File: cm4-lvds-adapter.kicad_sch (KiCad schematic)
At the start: 58 parts, among them J1 Plug_Molex_SlimStack_2x15_538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, J2 JST_SM_1x10_SM10B-SURS-TF-LF-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, J3 Conn_FFC_Amphenol_62684-40210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, U2 NTS0104_DHVQFN, U3 SN65DSI84

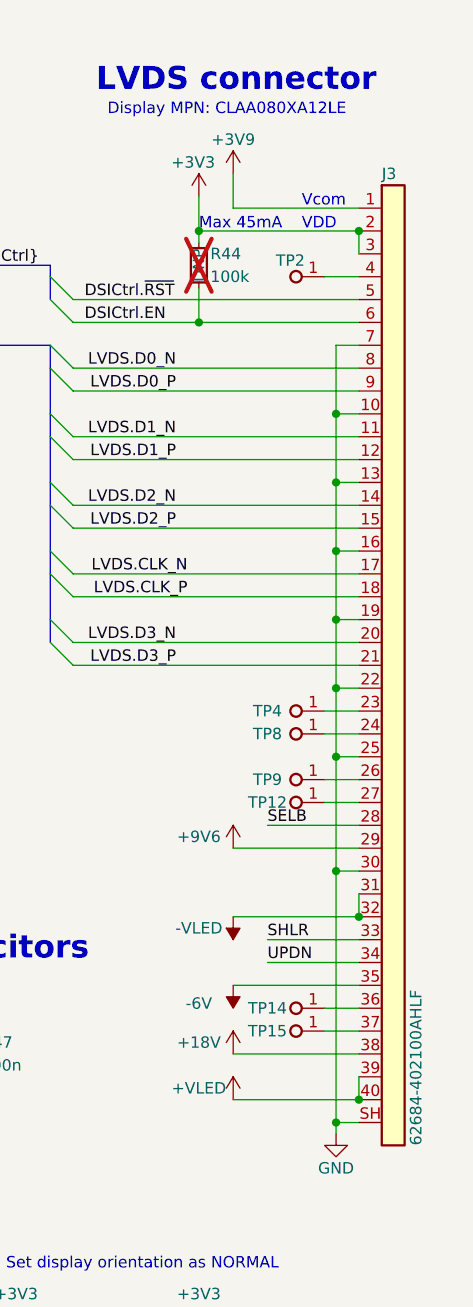
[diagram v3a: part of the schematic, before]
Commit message: [#55111] Change FFC on schematic
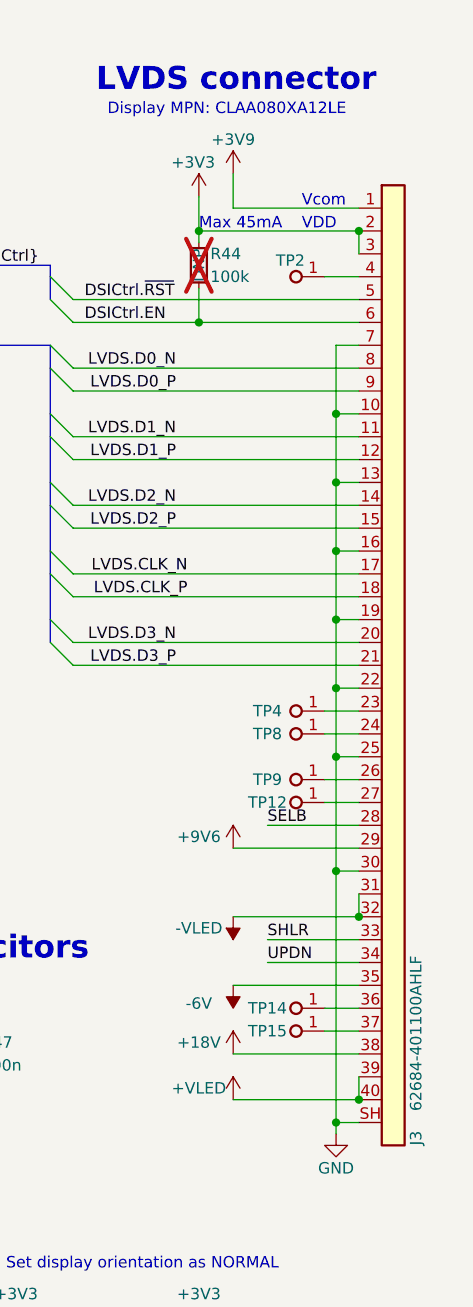
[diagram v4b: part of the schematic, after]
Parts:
- removed J3: Conn_FFC_Amphenol_62684-402100AHLF, antmicro-footprints:Conn_FFC_Amphenol_1x40_62684-402100AHLF, symbol antmicroFCCConnectors:FFC_Amphenol_1x40_62684-402100AHLF
- added J3: FFC_Amphenol_1x40_62684-401100AHLF, antmicro-footprints:Conn_FFC_Amphenol_1x40_62684-401100AHLF, symbol antmicroFCCConnectors:FFC_Amphenol_1x40_62684-401100AHLF
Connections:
- net +18V: now also J3.38
- net +3V3: now also J3.2, J3.3
- net +3V9: now also J3.1
- net +9V6: now also J3.29
- net +VLED: now also J3.39, J3.40
- net -6V: now also J3.35
- net -VLED: now also J3.31, J3.32
- net DSICtrl.EN: now also J3.6
- net DSICtrl.~{RST}: now also J3.5
- net GND: now also J3.10, J3.13, J3.16, J3.19, J3.22, J3.25, J3.30, J3.7, J3.SH
- net LVDS.CLK_N: now also J3.17
- net LVDS.CLK_P: now also J3.18
- net LVDS.D0_N: now also J3.8
- net LVDS.D0_P: now also J3.9
- net LVDS.D1_N: now also J3.11
- net LVDS.D1_P: now also J3.12
- net LVDS.D2_N: now also J3.14
- net LVDS.D2_P: now also J3.15
- net LVDS.D3_N: now also J3.20
- net LVDS.D3_P: now also J3.21
- net SELB: now also J3.28
- net SHLR: now also J3.33
- net UPDN: now also J3.34
- net at TP9.1: now also J3.26
- net at TP8.1: now also J3.24
- net at TP15.1: now also J3.37
- net at TP4.1: now also J3.23
- net at TP12.1: now also J3.27
- net at TP14.1: now also J3.36
- net at TP2.1: now also J3.4
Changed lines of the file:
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@@
   (junction (at 58.42 190.5) (diameter 0) (color 0 0 0 0)
   )
+  (junction (at 392.43 196.85) (diameter 0) (color 0 0 0 0)
+  )
   (junction (at 389.89 143.51) (diameter 0) (color 0 0 0 0)
   )
@@
   (junction (at 389.89 128.27) (diameter 0) (color 0 0 0 0)
   )
-  (junction (at 392.43 176.53) (diameter 0) (color 0 0 0 0)
-  )
   (junction (at 374.65 110.49) (diameter 0) (color 0 0 0 0)
   )
@@
   (junction (at 156.21 187.96) (diameter 0) (color 0 0 0 0)
   )
+  (junction (at 392.43 176.53) (diameter 0) (color 0 0 0 0)
+  )
   (junction (at 332.74 232.41) (diameter 0) (color 0 0 0 0)
   )
@@
   (junction (at 45.72 99.06) (diameter 0) (color 0 0 0 0)
   )
-  (junction (at 392.43 196.85) (diameter 0) (color 0 0 0 0)
-  )
   (junction (at 45.72 76.2) (diameter 0) (color 0 0 0 0)
   )
@@
     )
   )
-  (symbol (lib_id "antmicroFCCConnectors:FFC_Amphenol_1x40_62684-402100AHLF") (at 392.43 97.79 0) (unit 1)
-    (in_bom yes) (on_board yes) (dnp no)
-    (property "Reference" "J3" (at 394.97 93.98 0)
-      (effects (font (size 1.27 1.27) (thickness 0.15)) (justify left))
-    )
-    (property "Value" "Conn_FFC_Amphenol_62684-402100AHLF" (at 419.1 105.41 0)
-      (effects (font (size 1.27 1.27) (thickness 0.15)) (justify left bottom) hide)
-    )
-    (property "Footprint" "antmicro-footprints:Conn_FFC_Amphenol_1x40_62684-402100AHLF" (at 414.02 107.95 0)
-      (effects (font (size 1.27 1.27) (thickness 0.15)) (justify left bottom) hide)
-    )
-    (property "Datasheet" "https://cdn.amphenol-cs.com/media/wysiwyg/files/drawing/62684.pdf" (at 414.02 110.49 0)
-      (effects (font (size 1.27 1.27) (thickness 0.15)) (justify left bottom) hide)
-    )
-    (property "MPN" "62684-402100AHLF" (at 398.78 201.93 90)
-      (effects (font (size 1.27 1.27) (thickness 0.15)) (justify left))
-    )
-    (property "Manufacturer" "Amphenol" (at 414.02 113.03 0)
-      (effects (font (size 1.27 1.27) (thickness 0.15)) (justify left bottom) hide)
-    )
-    (property "Author" "Antmicro" (at 414.02 115.57 0)
-      (effects (font (size 1.27 1.27) (thickness 0.15)) (justify left bottom) hide)
-    )
-    (property "License" "Apache-2.0" (at 414.02 118.11 0)
-      (effects (font (size 1.27 1.27) (thickness 0.15)) (justify left bottom) hide)
-    )
-    (pin "1")
-    (pin "10")
-    (pin "11")
-    (pin "12")
-    (pin "13")
-    (pin "14")
-    (pin "15")
-    (pin "16")
-    (pin "17")
-    (pin "18")
-    (pin "19")
-    (pin "2")
-    (pin "20")
-    (pin "21")
-    (pin "22")
-    (pin "23")
-    (pin "24")
-    (pin "25")
-    (pin "26")
-    (pin "27")
-    (pin "28")
-    (pin "29")
-    (pin "3")
-    (pin "30")
-    (pin "31")
-    (pin "32")
-    (pin "33")
-    (pin "34")
-    (pin "35")
-    (pin "36")
-    (pin "37")
-    (pin "38")
-    (pin "39")
-    (pin "4")
-    (pin "40")
-    (pin "5")
-    (pin "6")
-    (pin "7")
-    (pin "8")
-    (pin "9")
-    (pin "SH")
-    (instances
-      (project "cm4-lvds-adapter"
-        (path "/60b842dc-0853-4a25-99ac-5784ddf94d0d"
-          (reference "J3") (unit 1)
-        )
-      )
-    )
-  )
   (symbol (lib_id "antmicropower:+VLED") (at 337.82 187.96 0) (unit 1)
     (in_bom yes) (on_board yes) (dnp no)
@@
         )
       )
+    )
+  )
+  (symbol (lib_id "antmicroFCCConnectors:FFC_Amphenol_1x40_62684-401100AHLF") (at 392.43 97.79 0) (unit 1)
+    (in_bom yes) (on_board yes) (dnp no)
+    (property "Reference" "J3" (at 398.78 201.93 90)
+      (effects (font (size 1.27 1.27) (thickness 0.15)) (justify left))
+    )
+    (property "Value" "FFC_Amphenol_1x40_62684-401100AHLF" (at 414.02 105.41 0)
+      (effects (font (size 1.27 1.27) (thickness 0.15)) (justify left bottom) hide)
+    )
+    (property "Footprint" "antmicro-footprints:Conn_FFC_Amphenol_1x40_62684-401100AHLF" (at 414.02 107.95 0)
+      (effects (font (size 1.27 1.27) (thickness 0.15)) (justify left bottom) hide)
+    )
+    (property "Datasheet" "https://cdn.amphenol-cs.com/media/wysiwyg/files/drawing/62684.pdf" (at 414.02 110.49 0)
+      (effects (font (size 1.27 1.27) (thickness 0.15)) (justify left bottom) hide)
+    )
+    (property "MPN" "62684-401100AHLF" (at 398.78 198.12 90)
+      (effects (font (size 1.27 1.27) (thickness 0.15)) (justify left))
+    )
+    (property "Manufacturer" "Amphenol" (at 414.02 113.03 0)
+      (effects (font (size 1.27 1.27) (thickness 0.15)) (justify left bottom) hide)
+    )
+    (property "Author" "Antmicro" (at 414.02 115.57 0)
+      (effects (font (size 1.27 1.27) (thickness 0.15)) (justify left bottom) hide)
+    )
+    (property "License" "Apache-2.0" (at 414.02 118.11 0)
+      (effects (font (size 1.27 1.27) (thickness 0.15)) (justify left bottom) hide)
+    )
+    (pin "26")
+    (pin "35")
+    (pin "37")
+    (pin "1")
+    (pin "39")
+    (pin "36")
+    (pin "6")
+    (pin "31")
+    (pin "21")
+    (pin "40")
+    (pin "12")
+    (pin "17")
+    (pin "34")
+    (pin "23")
+    (pin "8")
+    (pin "25")
+    (pin "19")
+    (pin "28")
+    (pin "16")
+    (pin "4")
+    (pin "2")
+    (pin "33")
+    (pin "38")
+    (pin "7")
+    (pin "9")
+    (pin "3")
+    (pin "20")
+    (pin "15")
+    (pin "18")
+    (pin "11")
+    (pin "29")
+    (pin "27")
+    (pin "13")
+    (pin "14")
+    (pin "32")
+    (pin "5")
+    (pin "24")
+    (pin "10")
+    (pin "30")
+    (pin "SH")
+    (pin "22")
+    (instances
+      (project "cm4-lvds-adapter"
+        (path "/60b842dc-0853-4a25-99ac-5784ddf94d0d"
+          (reference "J3") (unit 1)
+        )
+      )

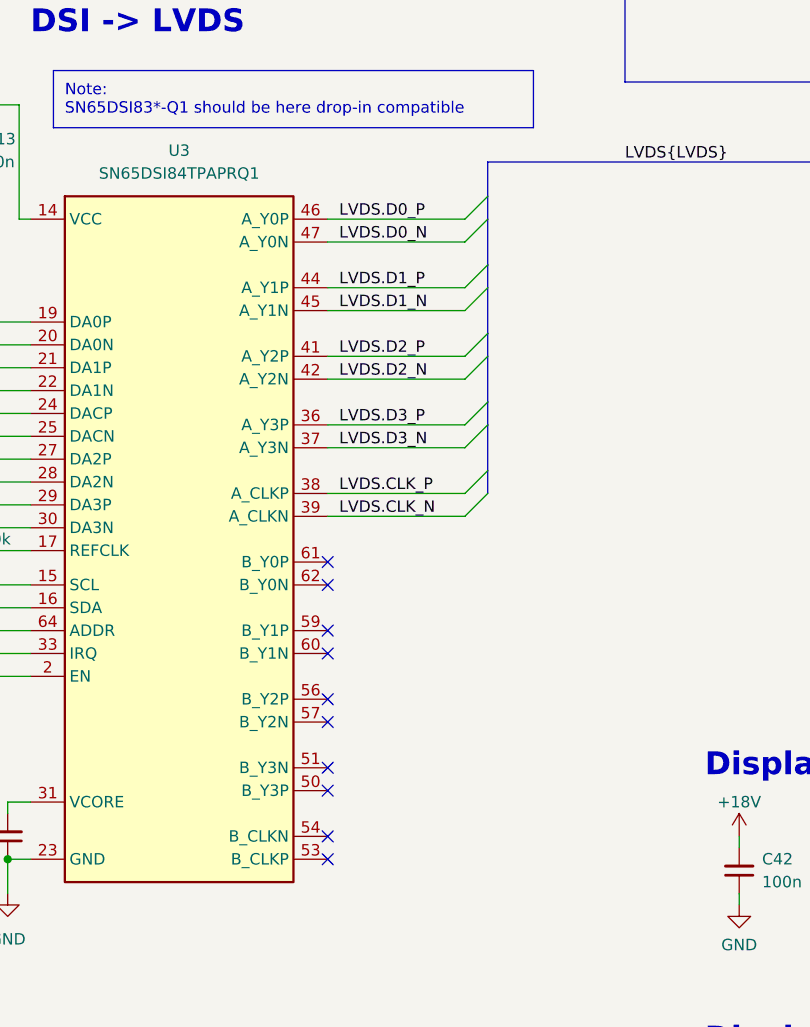
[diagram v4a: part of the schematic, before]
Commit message: [#55272] Change layout of the SN65DSI84-Q1
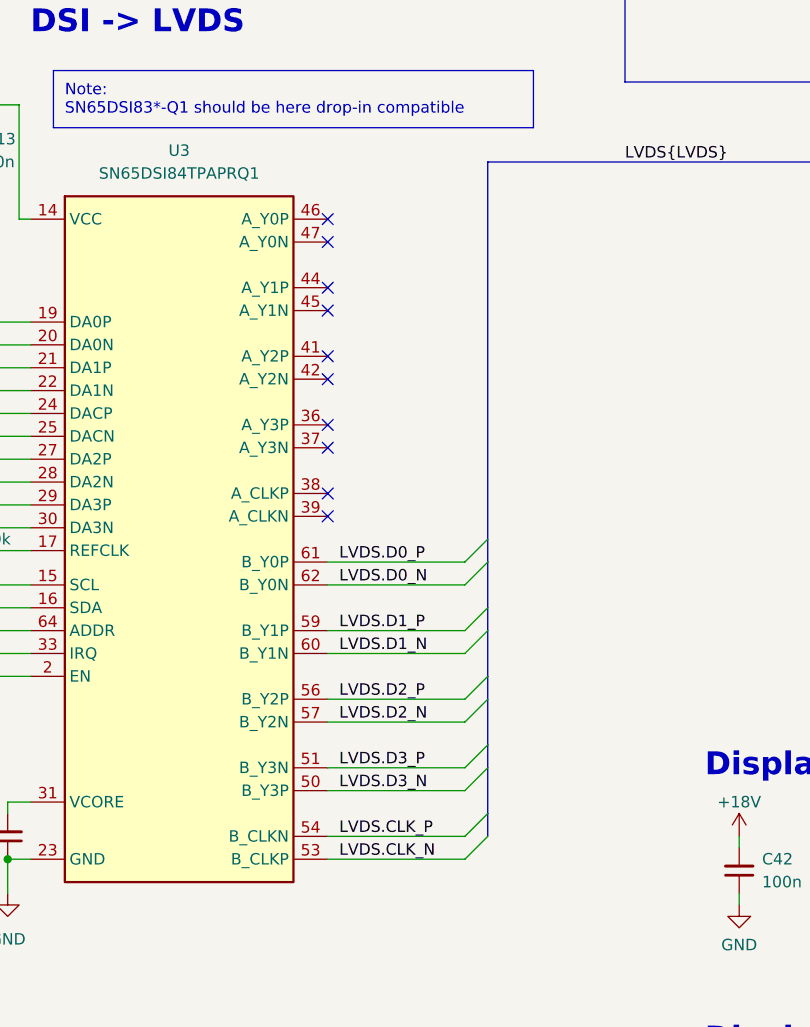
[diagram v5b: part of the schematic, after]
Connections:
- net LVDS.CLK_N: now also U3.53 (B_CLKP); no longer U3.39 (A_CLKN)
- net LVDS.CLK_P: now also U3.54 (B_CLKN); no longer U3.38 (A_CLKP)
- net LVDS.D0_N: now also U3.62 (B_Y0N); no longer U3.47 (A_Y0N)
- net LVDS.D0_P: now also U3.61 (B_Y0P); no longer U3.46 (A_Y0P)
- net LVDS.D1_N: now also U3.60 (B_Y1N); no longer U3.45 (A_Y1N)
- net LVDS.D1_P: now also U3.59 (B_Y1P); no longer U3.44 (A_Y1P)
- net LVDS.D2_N: now also U3.57 (B_Y2N); no longer U3.42 (A_Y2N)
- net LVDS.D2_P: now also U3.56 (B_Y2P); no longer U3.41 (A_Y2P)
- net LVDS.D3_N: now also U3.50 (B_Y3P); no longer U3.37 (A_Y3N)
- net LVDS.D3_P: now also U3.51 (B_Y3N); no longer U3.36 (A_Y3P)
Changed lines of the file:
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@@
   (no_connect (at 58.42 111.76))
   (no_connect (at 58.42 109.22))
-  (no_connect (at 261.62 157.48))
-  (no_connect (at 261.62 165.1))
-  (no_connect (at 261.62 180.34))
-  (no_connect (at 261.62 172.72))
-  (no_connect (at 261.62 175.26))
+  (no_connect (at 261.62 119.38))
+  (no_connect (at 261.62 127))
+  (no_connect (at 261.62 142.24))
+  (no_connect (at 261.62 134.62))
+  (no_connect (at 261.62 137.16))
   (no_connect (at 46.99 116.84))
   (no_connect (at 58.42 114.3))
   (no_connect (at 46.99 114.3))
-  (no_connect (at 261.62 182.88))
-  (no_connect (at 261.62 187.96))
+  (no_connect (at 261.62 144.78))
+  (no_connect (at 261.62 149.86))
   (no_connect (at 46.99 111.76))
-  (no_connect (at 261.62 160.02))
-  (no_connect (at 261.62 190.5))
+  (no_connect (at 261.62 121.92))
+  (no_connect (at 261.62 152.4))
   (no_connect (at 46.99 109.22))
-  (no_connect (at 261.62 167.64))
-  (bus_entry (at 279.4 124.46) (size -2.54 2.54)
+  (no_connect (at 261.62 129.54))
+  (bus_entry (at 279.4 162.56) (size -2.54 2.54)
     (stroke (width 0) (type default))
   )
@@
     (stroke (width 0) (type default))
   )
-  (bus_entry (at 279.4 116.84) (size -2.54 2.54)
+  (bus_entry (at 279.4 154.94) (size -2.54 2.54)
     (stroke (width 0) (type default))
   )
@@
     (stroke (width 0) (type default))
   )
-  (bus_entry (at 279.4 119.38) (size -2.54 2.54)
+  (bus_entry (at 279.4 157.48) (size -2.54 2.54)
     (stroke (width 0) (type default))
   )
@@
     (stroke (width 0) (type default))
   )
-  (bus_entry (at 279.4 149.86) (size -2.54 2.54)
+  (bus_entry (at 279.4 187.96) (size -2.54 2.54)
     (stroke (width 0) (type default))
   )
@@
     (stroke (width 0) (type default))
   )
-  (bus_entry (at 279.4 132.08) (size -2.54 2.54)
+  (bus_entry (at 279.4 170.18) (size -2.54 2.54)
     (stroke (width 0) (type default))
   )
-  (bus_entry (at 279.4 147.32) (size -2.54 2.54)
+  (bus_entry (at 279.4 185.42) (size -2.54 2.54)
     (stroke (width 0) (type default))
   )
@@
     (stroke (width 0) (type default))
   )
-  (bus_entry (at 279.4 127) (size -2.54 2.54)
+  (bus_entry (at 279.4 165.1) (size -2.54 2.54)
     (stroke (width 0) (type default))
   )
@@
     (stroke (width 0) (type default))
   )
-  (bus_entry (at 279.4 139.7) (size -2.54 2.54)
+  (bus_entry (at 279.4 177.8) (size -2.54 2.54)
     (stroke (width 0) (type default))
   )
@@
     (stroke (width 0) (type default))
   )
-  (bus_entry (at 279.4 142.24) (size -2.54 2.54)
+  (bus_entry (at 279.4 180.34) (size -2.54 2.54)
     (stroke (width 0) (type default))
   )
@@
     (stroke (width 0) (type default))
   )
-  (bus_entry (at 279.4 134.62) (size -2.54 2.54)
+  (bus_entry (at 279.4 172.72) (size -2.54 2.54)
     (stroke (width 0) (type default))
   )
@@
     (stroke (width 0) (type default))
   )
-  (wire (pts (xy 261.62 134.62) (xy 276.86 134.62))
+  (wire (pts (xy 261.62 172.72) (xy 276.86 172.72))
     (stroke (width 0) (type default))
   )
@@
     (stroke (width 0) (type default))
   )
-  (bus (pts (xy 279.4 116.84) (xy 279.4 119.38))
+  (bus (pts (xy 279.4 154.94) (xy 279.4 157.48))
     (stroke (width 0) (type default))
   )
@@
     (stroke (width 0) (type default))
   )
-  (wire (pts (xy 261.62 127) (xy 276.86 127))
+  (wire (pts (xy 261.62 165.1) (xy 276.86 165.1))
     (stroke (width 0) (type default))
   )
-  (bus (pts (xy 279.4 127) (xy 279.4 132.08))
+  (bus (pts (xy 279.4 165.1) (xy 279.4 170.18))
     (stroke (width 0) (type default))
   )
@@
     (stroke (width 0) (type default))
   )
-  (bus (pts (xy 279.4 119.38) (xy 279.4 124.46))
+  (bus (pts (xy 279.4 157.48) (xy 279.4 162.56))
     (stroke (width 0) (type default))
   )
@@
     (stroke (width 0) (type default))
   )
-  (bus (pts (xy 279.4 113.03) (xy 279.4 116.84))
+  (bus (pts (xy 279.4 113.03) (xy 279.4 154.94))
     (stroke (width 0) (type default))
   )
@@
     (stroke (width 0) (type default))
   )
-  (wire (pts (xy 261.62 149.86) (xy 276.86 149.86))
+  (wire (pts (xy 261.62 187.96) (xy 276.86 187.96))
     (stroke (width 0) (type default))
   )
@@
     (stroke (width 0) (type default))
   )
-  (wire (pts (xy 261.62 152.4) (xy 276.86 152.4))
+  (wire (pts (xy 261.62 190.5) (xy 276.86 190.5))
     (stroke (width 0) (type default))
   )
@@
     (stroke (width 0) (type default))
   )
-  (wire (pts (xy 261.62 129.54) (xy 276.86 129.54))
+  (wire (pts (xy 261.62 167.64) (xy 276.86 167.64))
     (stroke (width 0) (type default))
   )
@@
     (stroke (width 0) (type default))
   )
-  (bus (pts (xy 279.4 142.24) (xy 279.4 147.32))
+  (bus (pts (xy 279.4 180.34) (xy 279.4 185.42))
     (stroke (width 0) (type default))
   )
@@
     (stroke (width 0) (type default))
   )
-  (wire (pts (xy 261.62 119.38) (xy 276.86 119.38))
+  (wire (pts (xy 261.62 157.48) (xy 276.86 157.48))
     (stroke (width 0) (type default))
   )
@@
     (stroke (width 0) (type default))
   )
-  (bus (pts (xy 279.4 139.7) (xy 279.4 142.24))
+  (bus (pts (xy 279.4 177.8) (xy 279.4 180.34))
     (stroke (width 0) (type default))
   )
@@
     (stroke (width 0) (type default))
   )
-  (wire (pts (xy 261.62 121.92) (xy 276.86 121.92))
+  (wire (pts (xy 261.62 160.02) (xy 276.86 160.02))
     (stroke (width 0) (type default))
   )
@@
     (stroke (width 0) (type default))
   )
-  (bus (pts (xy 279.4 132.08) (xy 279.4 134.62))
+  (bus (pts (xy 279.4 170.18) (xy 279.4 172.72))
     (stroke (width 0) (type default))
   )
@@
     (stroke (width 0) (type default))
   )
-  (wire (pts (xy 261.62 144.78) (xy 276.86 144.78))
+  (wire (pts (xy 261.62 182.88) (xy 276.86 182.88))
     (stroke (width 0) (type default))
   )
@@
     (stroke (width 0) (type default))
   )
-  (wire (pts (xy 261.62 137.16) (xy 276.86 137.16))
+  (wire (pts (xy 261.62 175.26) (xy 276.86 175.26))
     (stroke (width 0) (type default))
   )
@@
     (stroke (width 0) (type default))
   )
-  (bus (pts (xy 279.4 134.62) (xy 279.4 139.7))
+  (bus (pts (xy 279.4 172.72) (xy 279.4 177.8))
     (stroke (width 0) (type default))
   )
@@
     (stroke (width 0) (type default))
   )
-  (bus (pts (xy 279.4 124.46) (xy 279.4 127))
+  (bus (pts (xy 279.4 162.56) (xy 279.4 165.1))
     (stroke (width 0) (type default))
   )
@@
     (stroke (width 0) (type default))
   )
-  (bus (pts (xy 279.4 147.32) (xy 279.4 149.86))
+  (bus (pts (xy 279.4 185.42) (xy 279.4 187.96))
     (stroke (width 0) (type default))
   )
@@
     (stroke (width 0) (type default))
   )
-  (wire (pts (xy 261.62 142.24) (xy 276.86 142.24))
+  (wire (pts (xy 261.62 180.34) (xy 276.86 180.34))
     (stroke (width 0) (type default))
   )
@@
     (effects (font (size 1.27 1.27)) (justify left bottom))
   )
-  (label "LVDS.D0_N" (at 262.89 121.92 0) (fields_autoplaced)
+  (label "LVDS.D0_N" (at 262.89 160.02 0) (fields_autoplaced)
     (effects (font (size 1.27 1.27)) (justify left bottom))
   )
@@
     (effects (font (size 1.27 1.27)) (justify left bottom))
   )
-  (label "LVDS.D0_P" (at 262.89 119.38 0) (fields_autoplaced)
+  (label "LVDS.D0_P" (at 262.89 157.48 0) (fields_autoplaced)
     (effects (font (size 1.27 1.27)) (justify left bottom))
   )
@@
     (effects (font (size 1.27 1.27)) (justify left bottom))
   )
-  (label "LVDS.D2_N" (at 262.89 137.16 0) (fields_autoplaced)
+  (label "LVDS.D2_N" (at 262.89 175.26 0) (fields_autoplaced)
     (effects (font (size 1.27 1.27)) (justify left bottom))
   )
@@
     (effects (font (size 1.27 1.27)) (justify right bottom))
   )
-  (label "LVDS.D3_P" (at 262.89 142.24 0) (fields_autoplaced)
+  (label "LVDS.D3_P" (at 262.89 180.34 0) (fields_autoplaced)
     (effects (font (size 1.27 1.27)) (justify left bottom))
   )
@@
     (effects (font (size 1.27 1.27)) (justify left bottom))
   )
-  (label "LVDS.D2_P" (at 262.89 134.62 0) (fields_autoplaced)
+  (label "LVDS.D2_P" (at 262.89 172.72 0) (fields_autoplaced)
     (effects (font (size 1.27 1.27)) (justify left bottom))
   )
@@
     (effects (font (size 1.27 1.27)) (justify left bottom))
   )
-  (label "LVDS.D1_N" (at 262.89 129.54 0) (fields_autoplaced)
+  (label "LVDS.D1_N" (at 262.89 167.64 0) (fields_autoplaced)
     (effects (font (size 1.27 1.27)) (justify left bottom))
   )
@@
     (effects (font (size 1.27 1.27)) (justify left bottom))
   )
-  (label "LVDS.CLK_P" (at 262.89 149.86 0) (fields_autoplaced)
+  (label "LVDS.CLK_P" (at 262.89 187.96 0) (fields_autoplaced)
     (effects (font (size 1.27 1.27)) (justify left bottom))
   )
@@
     (effects (font (size 1.27 1.27)) (justify right bottom))
   )
-  (label "LVDS.CLK_N" (at 262.89 152.4 0) (fields_autoplaced)
+  (label "LVDS.CLK_N" (at 262.89 190.5 0) (fields_autoplaced)
     (effects (font (size 1.27 1.27)) (justify left bottom))
   )
@@
     (effects (font (size 1.27 1.27)) (justify left bottom))
   )
-  (label "LVDS.D3_N" (at 262.89 144.78 0) (fields_autoplaced)
+  (label "LVDS.D3_N" (at 262.89 182.88 0) (fields_autoplaced)
     (effects (font (size 1.27 1.27)) (justify left bottom))
   )
@@
     (effects (font (size 1.27 1.27)) (justify left bottom))
   )
-  (label "LVDS.D1_P" (at 262.89 127 0) (fields_autoplaced)
+  (label "LVDS.D1_P" (at 262.89 165.1 0) (fields_autoplaced)
     (effects (font (size 1.27 1.27)) (justify left bottom))
   )
